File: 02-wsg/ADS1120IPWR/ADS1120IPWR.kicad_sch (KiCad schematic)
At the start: 3 parts, among them J1 Conn_01x08, J2 Conn_01x08, U1 ADS1120IPWR

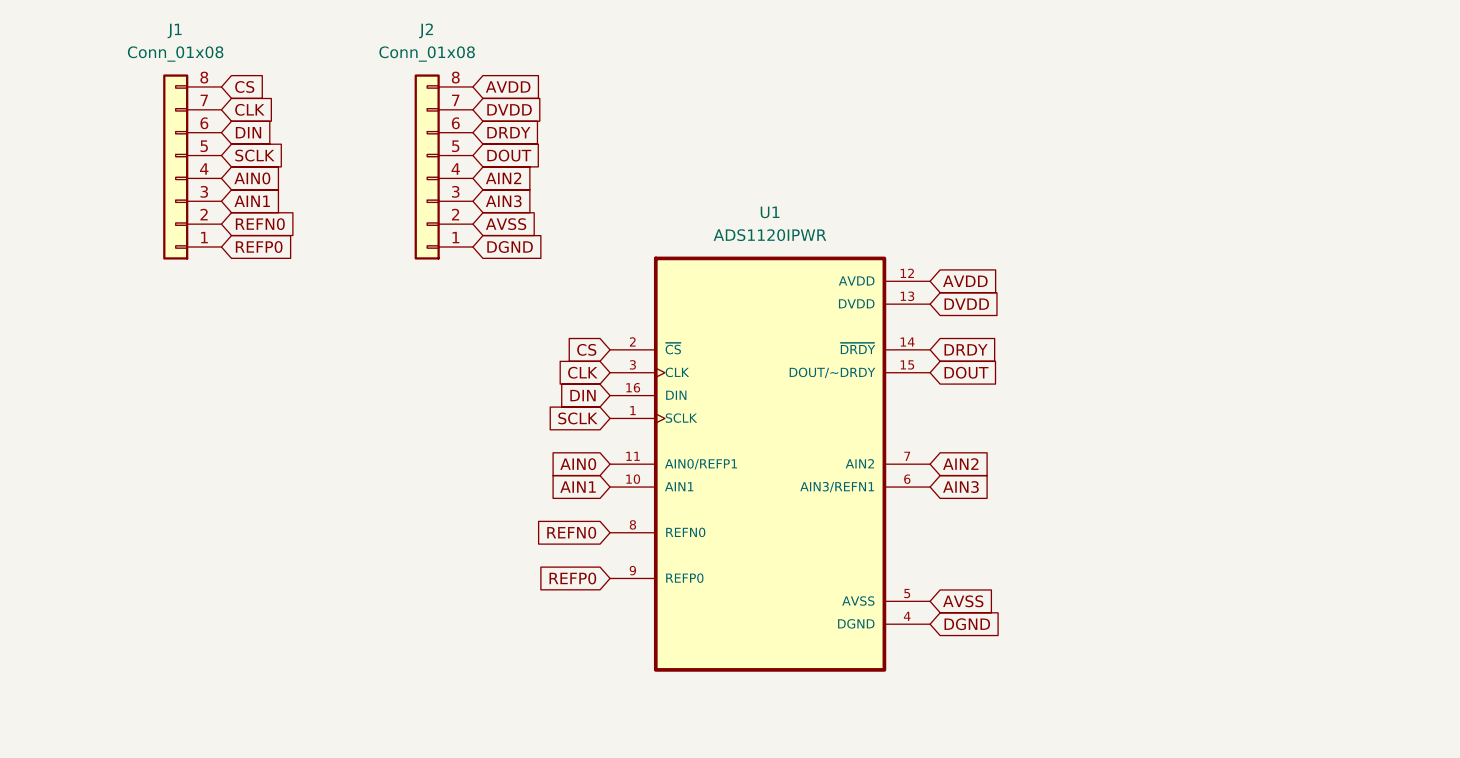
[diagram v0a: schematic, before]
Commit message: adc initial schematic
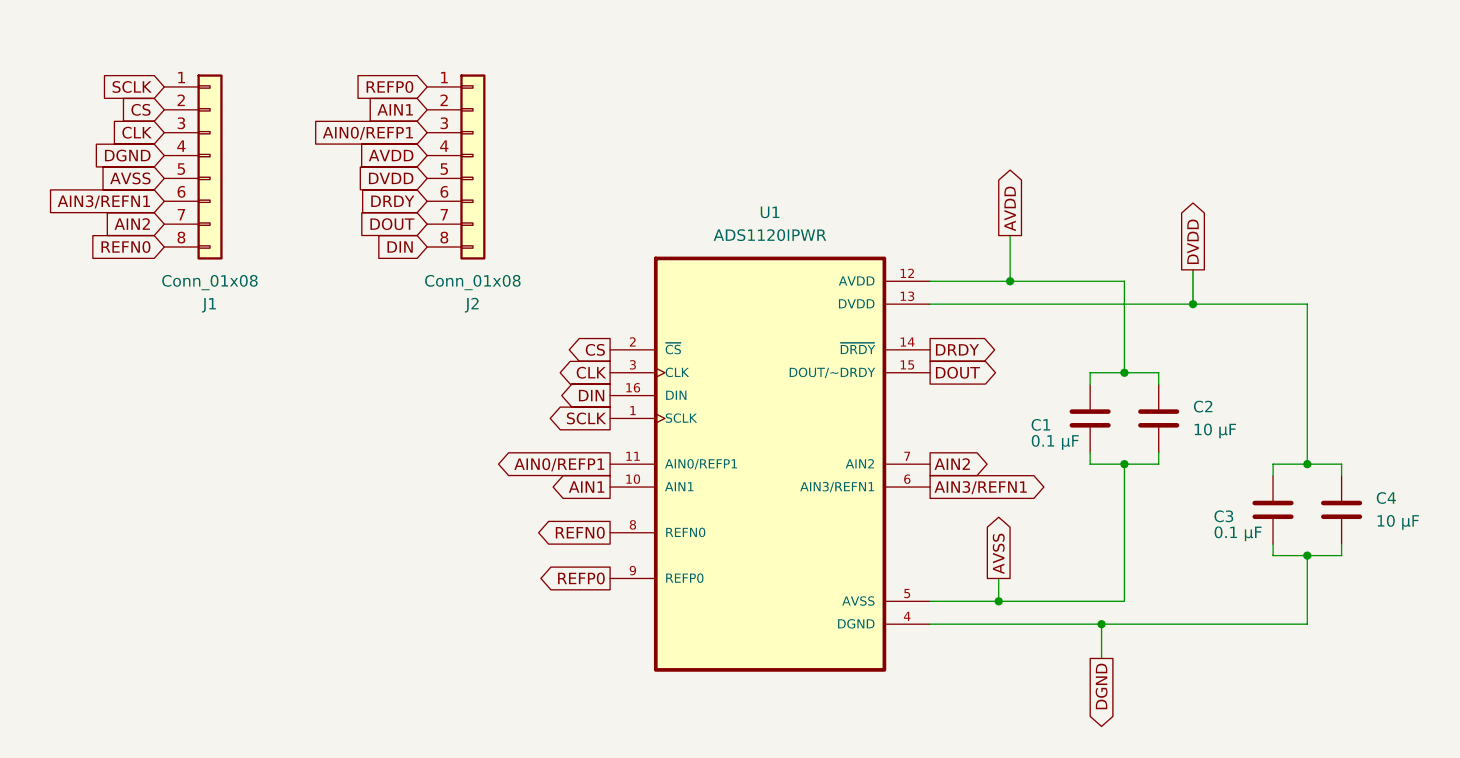
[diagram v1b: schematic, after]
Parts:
- added C1, C3: 0.1 μF, Capacitor_SMD:C_0201_0603Metric, symbol Device:C
- added C2, C4: 10 μF, Capacitor_SMD:C_0603_1608Metric, symbol Device:C
- J1, J2: footprint (none) -> Connector_PinHeader_2.54mm:PinHeader_1x08_P2.54mm_Vertical
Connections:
- net AIN1: now also J2.2 (Pin_2); no longer J1.3 (Pin_3)
- net AIN2: now also J1.7 (Pin_7); no longer J2.4 (Pin_4)
- net AVDD: now also J2.4 (Pin_4), C1.2, C2.1; no longer J2.8 (Pin_8)
- net AVSS: now also J1.5 (Pin_5), C1.1, C2.2; no longer J2.2 (Pin_2)
- net CLK: now also J1.3 (Pin_3); no longer J1.7 (Pin_7)
- net CS: now also J1.2 (Pin_2); no longer J1.8 (Pin_8)
- net DGND: now also J1.4 (Pin_4), C3.1, C4.2; no longer J2.1 (Pin_1)
- net DIN: now also J2.8 (Pin_8); no longer J1.6 (Pin_6)
- net DOUT: now also J2.7 (Pin_7); no longer J2.5 (Pin_5)
- net DVDD: now also J2.5 (Pin_5), C3.2, C4.1; no longer J2.7 (Pin_7)
- net REFN0: now also J1.8 (Pin_8); no longer J1.2 (Pin_2)
- net REFP0: now also J2.1 (Pin_1); no longer J1.1 (Pin_1)
- net SCLK: now also J1.1 (Pin_1); no longer J1.5 (Pin_5)
- net AIN0 renamed AIN0/REFP1
- net AIN0/REFP1: no longer J1.4 (Pin_4)
- net AIN3 renamed AIN0/REFP1
- net AIN0/REFP1: no longer U1.6 (AIN3/REFN1)
- new net AIN3/REFN1: U1.6 (AIN3/REFN1)
- new net AIN3/REFN1: J1.6 (Pin_6)
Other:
- moved on the sheet: J1, J2

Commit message: updated board
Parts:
- added NT1: NetTie_2, symbol Device:NetTie_2
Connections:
- net AVSS renamed GND
- net GND: now also NT1.2
- net CS renamed CS!
- net DGND renamed GNDD
- net GNDD: now also NT1.1
- net DRDY renamed DRDY!

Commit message: Changed WSG ADC breakout board size
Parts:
- C1, C3: footprint Capacitor_SMD:C_0201_0603Metric -> Capacitor_SMD:C_0402_1005Metric
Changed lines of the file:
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@@
 			)
 		)
-		(property "Footprint" "Capacitor_SMD:C_0201_0603Metric"
+		(property "Footprint" "Capacitor_SMD:C_0402_1005Metric"
 			(at 174.2948 54.61 0)
 			(effects
@@
 			)
 		)
-		(property "Footprint" "Capacitor_SMD:C_0201_0603Metric"
+		(property "Footprint" "Capacitor_SMD:C_0402_1005Metric"
 			(at 194.6148 64.77 0)
 			(effects
